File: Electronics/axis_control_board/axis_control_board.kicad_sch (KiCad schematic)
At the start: 8 parts, among them U1 IAP15W205S-35x-SOP16, U2 NRF24L01_Breakout, U3 AMS1117-3.3

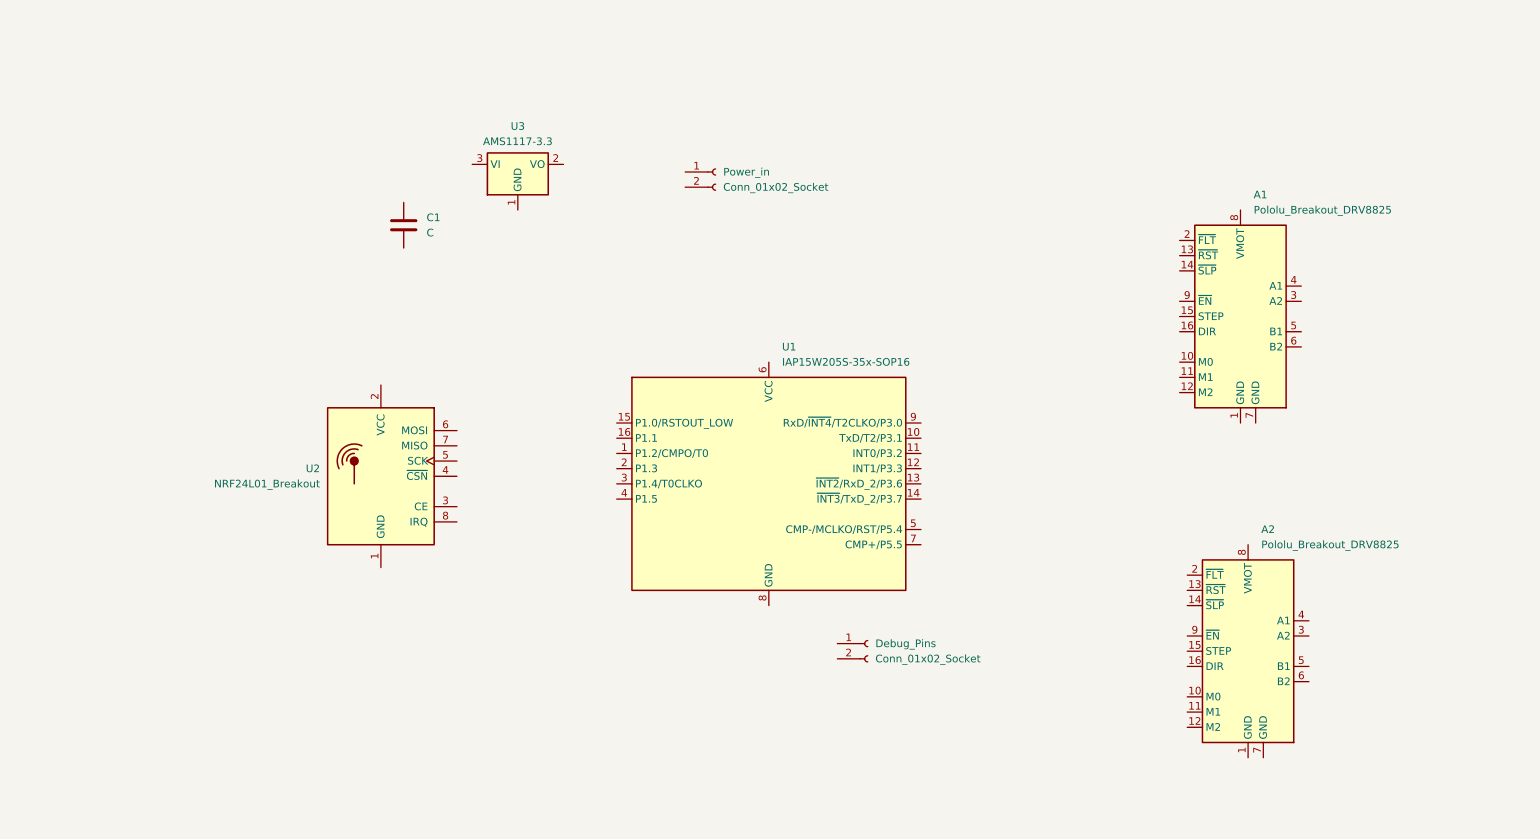
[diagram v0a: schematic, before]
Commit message: further development in axis control board
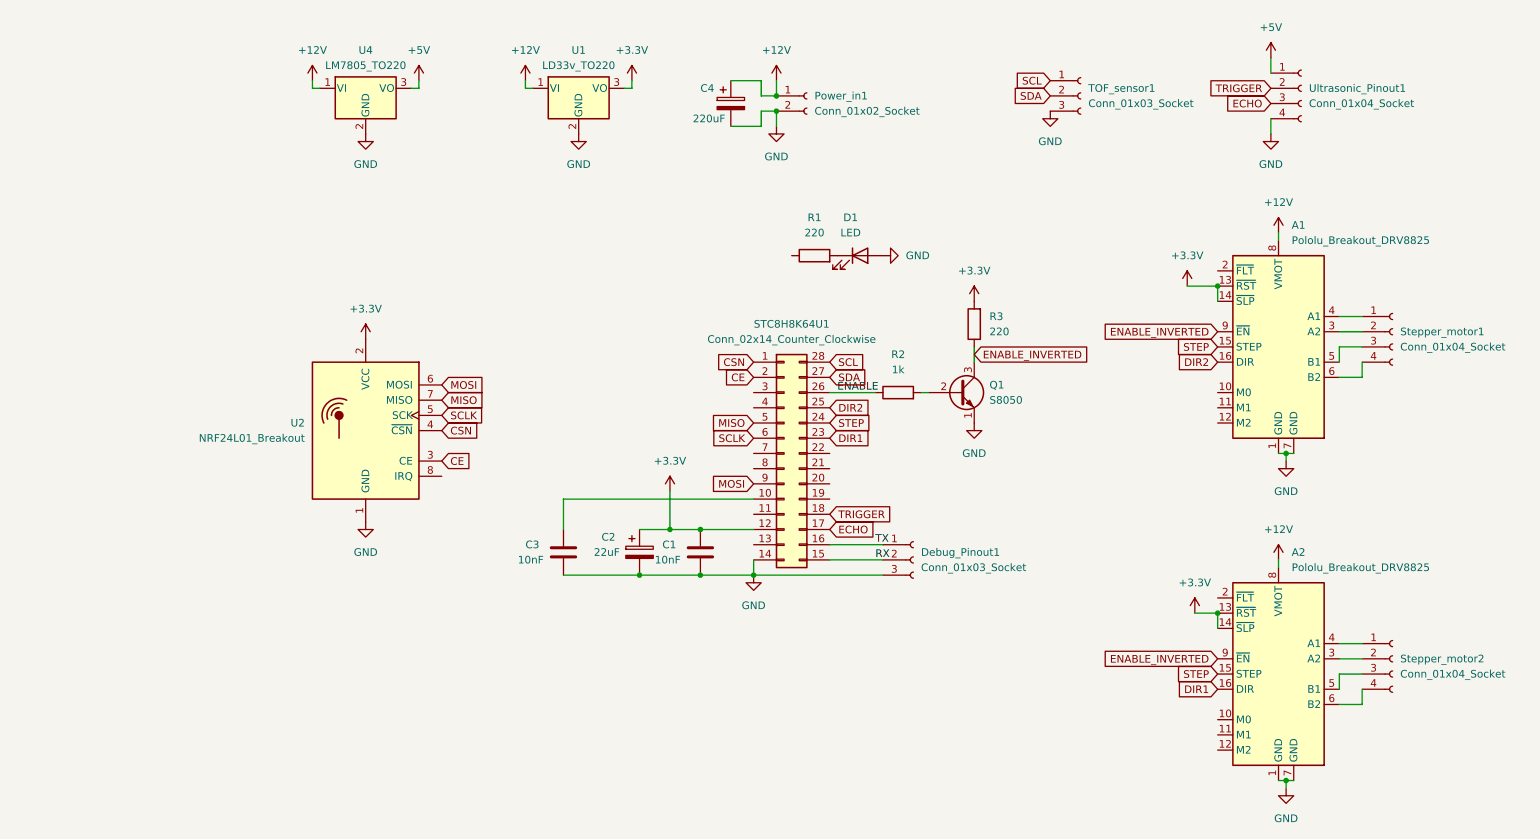
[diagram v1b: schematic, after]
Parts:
- removed Debug_Pins: Conn_01x02_Socket, Connector_PinSocket_2.54mm:PinSocket_1x02_P2.54mm_Horizontal, symbol Connector:Conn_01x02_Socket
- removed U1: IAP15W205S-35x-SOP16, Package_SO:STC_SOP-16_3.9x9.9mm_P1.27mm, symbol MCU_STC:IAP15W205S-35x-SOP16
- removed U3: AMS1117-3.3, Package_TO_SOT_SMD:SOT-223-3_TabPin2, symbol Regulator_Linear:AMS1117-3.3
- added C2: 22uF, Capacitor_THT:CP_Radial_D5.0mm_P2.00mm, symbol Device:C_Polarized
- added C3: 10nF, Capacitor_THT:C_Disc_D5.0mm_W2.5mm_P2.50mm, symbol Device:C
- added C4: 220uF, Capacitor_THT:CP_Radial_D5.0mm_P2.50mm, symbol Device:C_Polarized
- added D1: LED, LED_THT:LED_D3.0mm, symbol Device:LED
- added Debug_Pinout1, TOF_sensor1: Conn_01x03_Socket, Connector_PinSocket_2.54mm:PinSocket_1x03_P2.54mm_Vertical, symbol Connector:Conn_01x03_Socket
- added Q1: S8050, Package_TO_SOT_THT:TO-92_Inline, symbol Transistor_BJT:S8050
- added R1, R3: 220, Resistor_THT:R_Axial_DIN0207_L6.3mm_D2.5mm_P7.62mm_Horizontal, symbol Device:R
- added R2: 1k, Resistor_THT:R_Axial_DIN0207_L6.3mm_D2.5mm_P7.62mm_Horizontal, symbol Device:R
- added STC8H8K64U1: Conn_02x14_Counter_Clockwise, Package_DIP:DIP-28_W7.62mm_LongPads, symbol Connector_Generic:Conn_02x14_Counter_Clockwise
- added Stepper_motor1, Stepper_motor2, Ultrasonic_Pinout1: Conn_01x04_Socket, Connector_JST:JST_EH_B4B-EH-A_1x04_P2.50mm_Vertical, symbol Connector:Conn_01x04_Socket
- added U1: LD33v_TO220, Package_TO_SOT_THT:TO-220-3_Vertical, symbol Regulator_Linear:LM7805_TO220
- added U4: LM7805_TO220, Package_TO_SOT_THT:TO-220-3_Vertical, symbol Regulator_Linear:LM7805_TO220
- C1: value C -> 10nF; footprint (none) -> Capacitor_THT:C_Disc_D5.0mm_W2.5mm_P2.50mm
- renumbered Power_in to Power_in1
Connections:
- net GND: now reaches U2.1 (GND)
- net GND: now also A1.1 (GND), A1.7 (GND), A2.1 (GND), A2.7 (GND), C1.1, Power_in1.2 (Pin_2), C2.2, C3.1, C4.2, D1.2 (A), Debug_Pinout1.3 (Pin_3), Q1.1 (E), STC8H8K64U1.14 (Pin_14), TOF_sensor1.3 (Pin_3), U1.2 (GND), U4.2 (GND), Ultrasonic_Pinout1.4 (Pin_4)
- net +3.3V: now reaches U2.2 (VCC)
- net +3.3V: now also A1.13 (~{RST}), A1.14 (~{SLP}), A2.13 (~{RST}), A2.14 (~{SLP}), C1.2, C2.1, R3.2, STC8H8K64U1.12 (Pin_12), U1.3 (VO)
- net CE: now reaches U2.3 (CE)
- net CE: now also STC8H8K64U1.2 (Pin_2)
- net CSN: now reaches U2.4 (~{CSN})
- net CSN: now also STC8H8K64U1.1 (Pin_1)
- net SCLK: now reaches U2.5 (SCK)
- net SCLK: now also STC8H8K64U1.6 (Pin_6)
- net MOSI: now reaches U2.6 (MOSI)
- net MOSI: now also STC8H8K64U1.9 (Pin_9)
- net MISO: now reaches U2.7 (MISO)
- net MISO: now also STC8H8K64U1.5 (Pin_5)
- net +12V: now reaches Power_in1.1 (Pin_1)
- net +12V: now also A1.8 (VMOT), A2.8 (VMOT), C4.1, U1.1 (VI), U4.1 (VI)
- net STEP: now reaches A2.15 (STEP)
- net STEP: now also A1.15 (STEP), STC8H8K64U1.24 (Pin_24)
- net DIR1: now reaches A2.16 (DIR)
- net DIR1: now also STC8H8K64U1.23 (Pin_23)
- net at A2.3 (A2): now also Stepper_motor2.2 (Pin_2)
- net at A2.4 (A1): now also Stepper_motor2.1 (Pin_1)
- net at A2.5 (B1): now also Stepper_motor2.3 (Pin_3)
- net at A2.6 (B2): now also Stepper_motor2.4 (Pin_4)
- net ENABLE_INVERTED: now reaches A2.9 (~{EN})
- net ENABLE_INVERTED: now also A1.9 (~{EN}), Q1.3 (C), R3.1
- net DIR2: now reaches A1.16 (DIR)
- net DIR2: now also STC8H8K64U1.25 (Pin_25)
- net at A1.3 (A2): now also Stepper_motor1.2 (Pin_2)
- net at A1.4 (A1): now also Stepper_motor1.1 (Pin_1)
- net at A1.5 (B1): now also Stepper_motor1.3 (Pin_3)
- net at A1.6 (B2): now also Stepper_motor1.4 (Pin_4)
- new net: C3.2, STC8H8K64U1.10 (Pin_10)
- new net: Q1.2 (B), R2.2
- new net: D1.1 (K), R1.2
- new net +5V: U4.3 (VO), Ultrasonic_Pinout1.1 (Pin_1)
- new net ECHO: STC8H8K64U1.17 (Pin_17), Ultrasonic_Pinout1.3 (Pin_3)
- new net ENABLE: R2.1, STC8H8K64U1.26 (Pin_26)
- new net RX: Debug_Pinout1.2 (Pin_2), STC8H8K64U1.15 (Pin_15)
- new net SCL: STC8H8K64U1.28 (Pin_28), TOF_sensor1.1 (Pin_1)
- new net SDA: STC8H8K64U1.27 (Pin_27), TOF_sensor1.2 (Pin_2)
- new net TRIGGER: STC8H8K64U1.18 (Pin_18), Ultrasonic_Pinout1.2 (Pin_2)
- new net TX: Debug_Pinout1.1 (Pin_1), STC8H8K64U1.16 (Pin_16)
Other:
- moved on the sheet: A1, A2, C1, Power_in1, U2

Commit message: finished axis control PCB design
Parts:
- removed C3: 10nF, Capacitor_THT:C_Disc_D5.0mm_W2.5mm_P2.50mm, symbol Device:C
- added Bridge1, Bridge2, Bridge3, Bridge4: 0ohm, Resistor_THT:R_Axial_DIN0207_L6.3mm_D2.5mm_P7.62mm_Horizontal, symbol Device:R
- added H1, H2, H3, H4: MountingHole, MountingHole:MountingHole_3.2mm_M3_Pad_TopOnly, symbol Mechanical:MountingHole
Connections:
- net +3.3V: now also D1.2 (A), STC8H8K64U1.13 (Pin_13)
- net CE: now also STC8H8K64U1.11 (Pin_11); no longer STC8H8K64U1.2 (Pin_2)
- net CSN: now also STC8H8K64U1.8 (Pin_8); no longer STC8H8K64U1.1 (Pin_1)
- net GND: now also Bridge3.1, Bridge4.1, Bridge4.2; no longer D1.2 (A), Q1.1 (E)
- net MISO: now also Bridge1.2; no longer STC8H8K64U1.5 (Pin_5)
- net SCL: now also TOF_sensor1.2 (Pin_2); no longer TOF_sensor1.1 (Pin_1)
- net SCLK: now also Bridge2.2; no longer STC8H8K64U1.6 (Pin_6)
- net SDA: now also TOF_sensor1.1 (Pin_1); no longer TOF_sensor1.2 (Pin_2)
- net at Stepper_motor2.1 (Pin_1): now also A2.3 (A2); no longer A2.4 (A1)
- net at Stepper_motor2.2 (Pin_2): now also A2.4 (A1); no longer A2.3 (A2)
- net at R1.1: now also STC8H8K64U1.1 (Pin_1)
- net at Stepper_motor1.1 (Pin_1): now also A1.3 (A2); no longer A1.4 (A1)
- net at Stepper_motor1.2 (Pin_2): now also A1.4 (A1); no longer A1.3 (A2)
- new net: Bridge3.2, Q1.1 (E)
- new net: Bridge1.1, STC8H8K64U1.5 (Pin_5)
- new net: Bridge2.1, STC8H8K64U1.6 (Pin_6)
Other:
- moved on the sheet: D1, R1

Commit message: updated axis_control PCB and fixed hardware bug
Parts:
- removed U1: LD33v_TO220, Package_TO_SOT_THT:TO-220-3_Vertical, symbol Regulator_Linear:LM7805_TO220
- added Bridge5: 0ohm, Resistor_THT:R_Axial_DIN0207_L6.3mm_D2.5mm_P5.08mm_Vertical, symbol Device:R
- added U3: AMS1117-3.3, Package_TO_SOT_THT:TO-220-3_Vertical, symbol Regulator_Linear:AMS1117-3.3
- A1, A2: value Pololu_Breakout_DRV8825 -> DRV8825
- Debug_Pinout1, TOF_sensor1: value Conn_01x03_Socket -> 01x03
- Power_in1: value Conn_01x02_Socket -> JST-2P
- R2: value 1k -> 2k
- STC8H8K64U1: value Conn_02x14_Counter_Clockwise -> SKDIP28
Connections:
- net +12V: now also U3.3 (VI)
- net +3.3V: now also Bridge5.2
- net CSN: now also STC8H8K64U1.2 (Pin_2); no longer STC8H8K64U1.8 (Pin_8)
- net GND: now also U3.1 (GND)
- new net: Bridge5.1, U3.2 (VO)
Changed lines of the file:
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@@
     (stroke (width 0) (type default))
   )
-  (wire (pts (xy 105.41 24.13) (xy 105.41 25.4))
+  (wire (pts (xy 104.14 26.67) (xy 104.14 27.94))
     (stroke (width 0) (type default))
   )
@@
     (stroke (width 0) (type default))
   )
-  (wire (pts (xy 123.19 24.13) (xy 123.19 25.4))
+  (wire (pts (xy 121.92 26.67) (xy 121.92 27.94))
     (stroke (width 0) (type default))
   )
@@
     (stroke (width 0) (type default))
   )
-  (wire (pts (xy 123.19 25.4) (xy 121.92 25.4))
+  (wire (pts (xy 121.92 27.94) (xy 120.65 27.94))
     (stroke (width 0) (type default))
   )
@@
     (stroke (width 0) (type default))
   )
-  (wire (pts (xy 106.68 25.4) (xy 105.41 25.4))
+  (wire (pts (xy 105.41 27.94) (xy 104.14 27.94))
     (stroke (width 0) (type default))
   )
@@
     )
   )
-  (global_label "CSN" (shape input) (at 143.51 88.9 180) (fields_autoplaced)
+  (global_label "CSN" (shape input) (at 143.51 73.66 180) (fields_autoplaced)
     (effects (font (size 1.27 1.27)) (justify right))
-    (property "Intersheetrefs" "${INTERSHEET_REFS}" (at 136.7148 88.9 0)
+    (property "Intersheetrefs" "${INTERSHEET_REFS}" (at 136.7148 73.66 0)
       (effects (font (size 1.27 1.27)) (justify right) hide)
     )
@@
     )
   )
-  (symbol (lib_id "power:+12V") (at 105.41 24.13 0) (unit 1)
-    (in_bom yes) (on_board yes) (dnp no) (fields_autoplaced)
-    (property "Reference" "#PWR016" (at 105.41 27.94 0)
-      (effects (font (size 1.27 1.27)) hide)
-    )
-    (property "Value" "+12V" (at 105.41 19.05 0)
-      (effects (font (size 1.27 1.27)))
-    )
-    (property "Footprint" "" (at 105.41 24.13 0)
-      (effects (font (size 1.27 1.27)) hide)
-    )
-    (property "Datasheet" "" (at 105.41 24.13 0)
+  (symbol (lib_id "power:+12V") (at 104.14 26.67 0) (unit 1)
+    (in_bom yes) (on_board yes) (dnp no) (fields_autoplaced)
+    (property "Reference" "#PWR016" (at 104.14 30.48 0)
+      (effects (font (size 1.27 1.27)) hide)
+    )
+    (property "Value" "+12V" (at 104.14 21.59 0)
+      (effects (font (size 1.27 1.27)))
+    )
+    (property "Footprint" "" (at 104.14 26.67 0)
+      (effects (font (size 1.27 1.27)) hide)
+    )
+    (property "Datasheet" "" (at 104.14 26.67 0)
       (effects (font (size 1.27 1.27)) hide)
     )
@@
     )
   )
-  (symbol (lib_id "power:+3.3V") (at 123.19 24.13 0) (unit 1)
-    (in_bom yes) (on_board yes) (dnp no) (fields_autoplaced)
-    (property "Reference" "#PWR04" (at 123.19 27.94 0)
-      (effects (font (size 1.27 1.27)) hide)
-    )
-    (property "Value" "+3.3V" (at 123.19 19.05 0)
-      (effects (font (size 1.27 1.27)))
-    )
-    (property "Footprint" "" (at 123.19 24.13 0)
-      (effects (font (size 1.27 1.27)) hide)
-    )
-    (property "Datasheet" "" (at 123.19 24.13 0)
+  (symbol (lib_id "power:+3.3V") (at 121.92 19.05 0) (unit 1)
+    (in_bom yes) (on_board yes) (dnp no) (fields_autoplaced)
+    (property "Reference" "#PWR04" (at 121.92 22.86 0)
+      (effects (font (size 1.27 1.27)) hide)
+    )
+    (property "Value" "+3.3V" (at 121.92 13.97 0)
+      (effects (font (size 1.27 1.27)))
+    )
+    (property "Footprint" "" (at 121.92 19.05 0)
+      (effects (font (size 1.27 1.27)) hide)
+    )
+    (property "Datasheet" "" (at 121.92 19.05 0)
       (effects (font (size 1.27 1.27)) hide)
     )
@@
     )
   )
+  (symbol (lib_id "Regulator_Linear:AMS1117-3.3") (at 113.03 27.94 0) (unit 1)
+    (in_bom yes) (on_board yes) (dnp no) (fields_autoplaced)
+    (property "Reference" "U3" (at 113.03 21.59 0)
+      (effects (font (size 1.27 1.27)))
+    )
+    (property "Value" "AMS1117-3.3" (at 113.03 24.13 0)
+      (effects (font (size 1.27 1.27)))
+    )
+    (property "Footprint" "Package_TO_SOT_THT:TO-220-3_Vertical" (at 113.03 22.86 0)
+      (effects (font (size 1.27 1.27)) hide)
+    )
+    (property "Datasheet" "http://www.advanced-monolithic.com/pdf/ds1117.pdf" (at 115.57 34.29 0)
+      (effects (font (size 1.27 1.27)) hide)
+    )
+    (pin "2")
+    (pin "1")
+    (pin "3")
+    (instances
+      (project "axis_control_board"
+        (path "/c464bac3-01d0-4f14-8423-fe4a2abbcdb1"
+          (reference "U3") (unit 1)
+        )
+      )
+    )
+  )
   (symbol (lib_id "power:GND") (at 143.51 106.68 0) (unit 1)
     (in_bom yes) (on_board yes) (dnp no) (fields_autoplaced)
@@
       (effects (font (size 1.27 1.27)) (justify left))
     )
-    (property "Value" "Conn_01x03_Socket" (at 199.39 27.94 0)
+    (property "Value" "01x03" (at 199.39 27.94 0)
       (effects (font (size 1.27 1.27)) (justify left))
     )
@@
       (effects (font (size 1.27 1.27)))
     )
-    (property "Value" "1k" (at 167.64 72.39 90)
+    (property "Value" "2k" (at 167.64 72.39 90)
       (effects (font (size 1.27 1.27)))
     )
@@
     )
   )
-  (symbol (lib_id "Regulator_Linear:LM7805_TO220") (at 114.3 25.4 0) (unit 1)
-    (in_bom yes) (on_board yes) (dnp no) (fields_autoplaced)
-    (property "Reference" "U1" (at 114.3 19.05 0)
-      (effects (font (size 1.27 1.27)))
-    )
-    (property "Value" "LD33v_TO220" (at 114.3 21.59 0)
-      (effects (font (size 1.27 1.27)))
-    )
-    (property "Footprint" "Package_TO_SOT_THT:TO-220-3_Vertical" (at 114.3 19.685 0)
-      (effects (font (size 1.27 1.27) italic) hide)
-    )
-    (property "Datasheet" "https://www.onsemi.cn/PowerSolutions/document/MC7800-D.PDF" (at 114.3 26.67 0)
-      (effects (font (size 1.27 1.27)) hide)
-    )
-    (pin "1")
-    (pin "2")
-    (pin "3")
-    (instances
-      (project "axis_control_board"
-        (path "/c464bac3-01d0-4f14-8423-fe4a2abbcdb1"
-          (reference "U1") (unit 1)
-        )
-      )
-    )
-  )
   (symbol (lib_id "Connector:Conn_01x02_Socket") (at 152.4 26.67 0) (unit 1)
     (in_bom yes) (on_board yes) (dnp no) (fields_autoplaced)
@@
       (effects (font (size 1.27 1.27)) (justify left))
     )
-    (property "Value" "Conn_01x02_Socket" (at 153.67 29.21 0)
+    (property "Value" "JST-2P" (at 153.67 29.21 0)
       (effects (font (size 1.27 1.27)) (justify left))
     )
@@
       (effects (font (size 1.27 1.27)) (justify left))
     )
-    (property "Value" "Pololu_Breakout_DRV8825" (at 233.3341 105.41 0)
+    (property "Value" "DRV8825" (at 233.3341 105.41 0)
       (effects (font (size 1.27 1.27)) (justify left))
     )
@@
     )
   )
-  (symbol (lib_id "power:GND") (at 114.3 33.02 0) (unit 1)
-    (in_bom yes) (on_board yes) (dnp no) (fields_autoplaced)
-    (property "Reference" "#PWR014" (at 114.3 39.37 0)
-      (effects (font (size 1.27 1.27)) hide)
-    )
-    (property "Value" "GND" (at 114.3 38.1 0)
-      (effects (font (size 1.27 1.27)))
-    )
-    (property "Footprint" "" (at 114.3 33.02 0)
-      (effects (font (size 1.27 1.27)) hide)
-    )
-    (property "Datasheet" "" (at 114.3 33.02 0)
+  (symbol (lib_id "power:GND") (at 113.03 35.56 0) (unit 1)
+    (in_bom yes) (on_board yes) (dnp no) (fields_autoplaced)
+    (property "Reference" "#PWR014" (at 113.03 41.91 0)
+      (effects (font (size 1.27 1.27)) hide)
+    )
+    (property "Value" "GND" (at 113.03 40.64 0)
+      (effects (font (size 1.27 1.27)))
+    )
+    (property "Footprint" "" (at 113.03 35.56 0)
+      (effects (font (size 1.27 1.27)) hide)
+    )
+    (property "Datasheet" "" (at 113.03 35.56 0)
       (effects (font (size 1.27 1.27)) hide)
     )
@@
     )
   )
+  (symbol (lib_id "Device:R") (at 121.92 22.86 180) (unit 1)
+    (in_bom yes) (on_board yes) (dnp no)
+    (property "Reference" "Bridge5" (at 124.46 22.86 90)
+      (effects (font (size 1.27 1.27)))
+    )
+    (property "Value" "0ohm" (at 123.19 22.86 90)
+      (effects (font (size 1.27 1.27)))
+    )
+    (property "Footprint" "Resistor_THT:R_Axial_DIN0207_L6.3mm_D2.5mm_P5.08mm_Vertical" (at 123.698 22.86 90)
+      (effects (font (size 1.27 1.27)) hide)
+    )
+    (property "Datasheet" "~" (at 121.92 22.86 0)
+      (effects (font (size 1.27 1.27)) hide)
+    )
+    (pin "1")
+    (pin "2")
+    (instances
+      (project "axis_control_board"
+        (path "/c464bac3-01d0-4f14-8423-fe4a2abbcdb1"
+          (reference "Bridge5") (unit 1)
+        )
+      )
+    )
+  )
   (symbol (lib_id "Connector:Conn_01x03_Socket") (at 170.18 104.14 0) (unit 1)
     (in_bom yes) (on_board yes) (dnp no) (fields_autoplaced)
@@
       (effects (font (size 1.27 1.27)) (justify left))
     )
-    (property "Value" "Conn_01x03_Socket" (at 171.45 105.41 0)
+    (property "Value" "01x03" (at 171.45 105.41 0)
       (effects (font (size 1.27 1.27)) (justify left))
     )
@@
       (effects (font (size 1.27 1.27)))
     )
-    (property "Value" "Conn_02x14_Counter_Clockwise" (at 149.86 67.31 0)
+    (property "Value" "SKDIP28" (at 149.86 67.31 0)
       (effects (font (size 1.27 1.27)))
     )
@@
       (effects (font (size 1.27 1.27)) (justify left))
     )
-    (property "Value" "Pololu_Breakout_DRV8825" (at 233.3341 50.8 0)
-      (effects (font (size 1.27 1.27)) (justify left))
-    )
+    (property "Value" "DRV8825" (at 233.3341 50.8 0)
+      (effects (font (size 1.27 1.27)) (justify left))
+    )
